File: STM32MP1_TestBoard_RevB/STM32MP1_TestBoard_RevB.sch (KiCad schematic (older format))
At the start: 0 parts

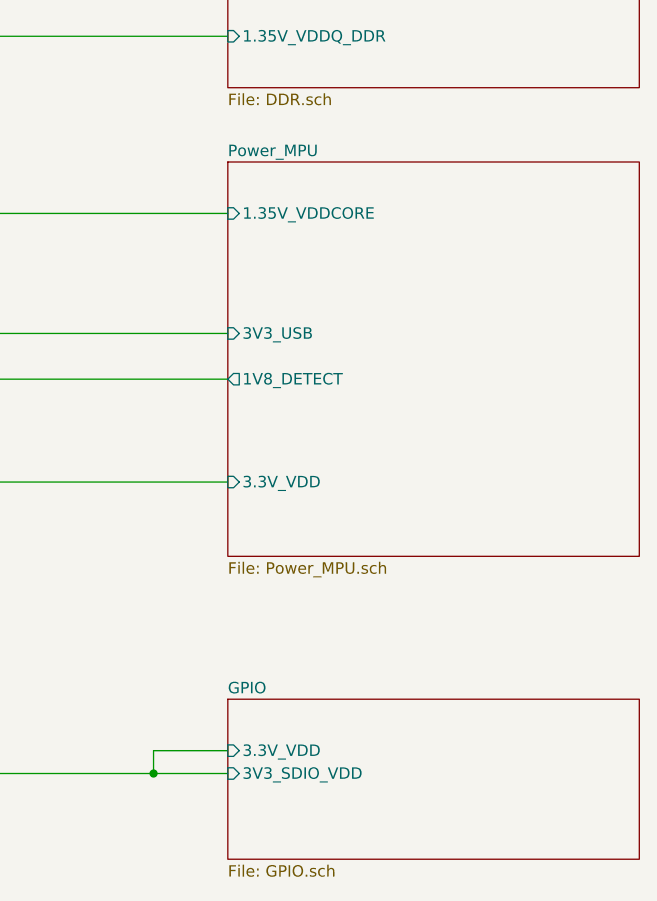
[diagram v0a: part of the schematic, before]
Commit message: Updated design
- Added Crystal/Oscillators
- Replaced both SDMMC with single SDMMC w/ detect pin
- Added USB Type C for VIN
- Moved SWD pins
- Tidied up silk screen for pin headers J1, J2, J3, J4
- Moved DSI socket
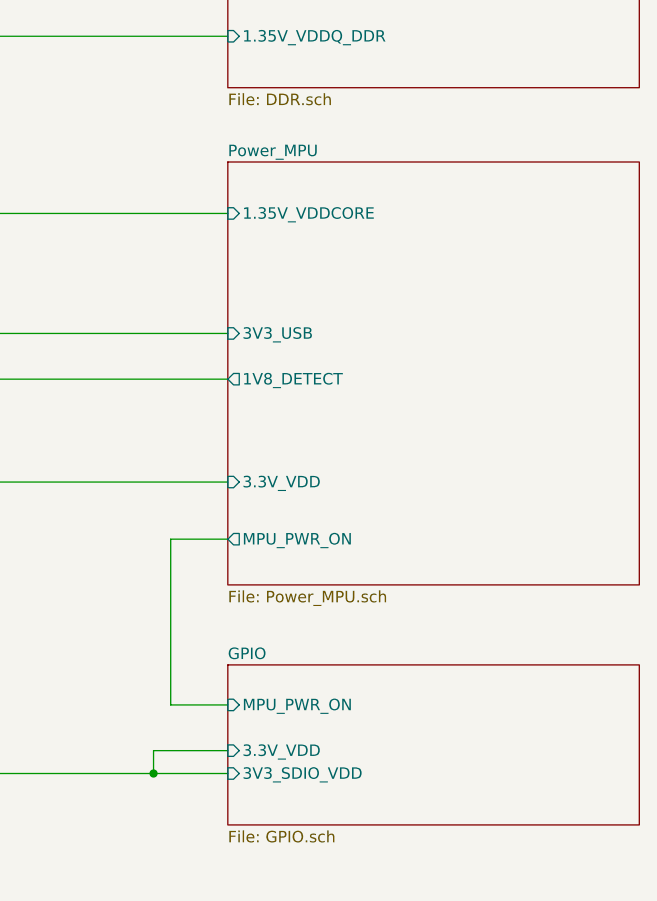
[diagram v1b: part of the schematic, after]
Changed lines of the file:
@@
 $Descr A3 16535 11693
 encoding utf-8
-Sheet 1 10
+Sheet 1 9
 Title ""
 Date "2021-03-15"
@@
 $EndDescr
 $Sheet
-S 9350 4275 1800 1725
+S 9350 4275 1800 1850
 U 6044C48A
 F0 "Power_MPU" 50
@@
 F4 "3.3V_VDD" I L 9350 5675 50
 F5 "1V8_DETECT" O L 9350 5225 50
+F6 "MPU_PWR_ON" O L 9350 5925 50
 $EndSheet
 Wire Wire Line
@@
 	9350 5025 6050 5025
 $Sheet
-S 9350 6625 1800 700
+S 9350 6475 1800 700
 U 6097C138
 F0 "GPIO" 50
@@
 F2 "3V3_SDIO_VDD" I L 9350 6950 50
 F3 "3.3V_VDD" I L 9350 6850 50
+F4 "MPU_PWR_ON" I L 9350 6650 50
 $EndSheet
+Wire Wire Line
+	9350 6650 9100 6650
+Wire Wire Line
+	9100 6650 9100 5925
+Wire Wire Line
+	9100 5925 9350 5925
 $EndSCHEMATC
